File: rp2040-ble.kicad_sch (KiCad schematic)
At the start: 38 parts, among them J1 Conn_01x15, J2 Conn_01x15, J3 USB_B_Micro, J4 Conn_01x03, SW1 SW_Push, SW2 SW_Push, U1 RP2040, U2 W25Q128JVS, U3 HM-BT4502, U4 NCP1117DT33G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

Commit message: WIP Routing
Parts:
- removed R3: DNP, Resistor_SMD:R_0603_1608Metric, symbol Device:R_Small
- removed Y1: 12MHz, Crystal:Crystal_SMD_Abracon_ABM3-2Pin_5.0x3.2mm_HandSoldering, symbol Device:Crystal
- added H1, H2, H3, H4: MountingHole, MountingHole:MountingHole_2.2mm_M2, symbol Mechanical:MountingHole
- added Y1: ABLS-12.000MHZ-B4-T, ABLS-12:XTAL_ABLS-12.000MHZ-B4-T, symbol ABLS-12.000MHZ-B4-T:ABLS-12.000MHZ-B4-T
- C1, C10, C11, C12, C13, C14, C2, C3, C4, C5, C6, C7, C8, C9: footprint Capacitor_SMD:C_0603_1608Metric -> Capacitor_SMD:C_0402_1005Metric
- J1, J2: footprint Connector_PinSocket_1.27mm:PinSocket_1x15_P1.27mm_Vertical -> Connector_PinSocket_2.54mm:PinSocket_1x15_P2.54mm_Vertical
- J4: footprint Connector_PinSocket_1.27mm:PinSocket_1x03_P1.27mm_Vertical -> Connector_PinHeader_1.27mm:PinHeader_1x03_P1.27mm_Vertical
- R1, R2, R4, R5, R6, R7, R8: footprint Resistor_SMD:R_0603_1608Metric -> Resistor_SMD:R_0402_1005Metric
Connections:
- net BLE_INT: now also U1.14 (GPIO11); no longer U1.6 (GPIO4)
- net BLE_POWER_DOWN: now also U1.18 (GPIO15); no longer U1.5 (GPIO3)
- net BLE_RX: now also U1.15 (GPIO12); no longer U1.2 (GPIO0)
- net BLE_TX: now also U1.16 (GPIO13); no longer U1.3 (GPIO1)
- net BLE_WAKEUP: now also U1.17 (GPIO14); no longer U1.4 (GPIO2)
- net GND: now also J1.13 (Pin_13), J1.14 (Pin_14); no longer J2.14 (Pin_14), J2.3 (Pin_3), J2.4 (Pin_4)
- net GPIO10: now also J1.12 (Pin_12); no longer J1.6 (Pin_6)
- net GPIO16: now also J2.14 (Pin_14)
- net GPIO17: now also J2.13 (Pin_13); no longer J1.12 (Pin_12)
- net GPIO18: now also J2.12 (Pin_12); no longer J1.13 (Pin_13)
- net GPIO19: now also J2.11 (Pin_11); no longer J1.14 (Pin_14)
- net GPIO20: now also J2.10 (Pin_10); no longer J2.5 (Pin_5)
- net GPIO21: now also J2.9 (Pin_9); no longer J2.6 (Pin_6)
- net GPIO22: now also J2.8 (Pin_8); no longer J2.7 (Pin_7)
- net GPIO23: now also J2.7 (Pin_7); no longer J2.8 (Pin_8)
- net GPIO24: now also J2.6 (Pin_6); no longer J2.9 (Pin_9)
- net GPIO26: now also J2.5 (Pin_5); no longer J2.10 (Pin_10)
- net GPIO27: now also J2.4 (Pin_4); no longer J2.11 (Pin_11)
- net GPIO28: now also J2.3 (Pin_3); no longer J2.12 (Pin_12)
- net GPIO29: now also J2.1 (Pin_1); no longer J2.13 (Pin_13)
- net GPIO5: now also J1.7 (Pin_7); no longer J1.1 (Pin_1)
- net GPIO6: now also J1.8 (Pin_8); no longer J1.2 (Pin_2)
- net GPIO7: now also J1.9 (Pin_9); no longer J1.3 (Pin_3)
- net GPIO8: now also J1.10 (Pin_10); no longer J1.4 (Pin_4)
- net GPIO9: now also J1.11 (Pin_11); no longer J1.5 (Pin_5)
- net SWCLK: now also J4.3 (Pin_3); no longer J4.1 (Pin_1)
- net SWD: now also J4.1 (Pin_1); no longer J4.3 (Pin_3)
- net VBUS: now also J1.1 (Pin_1); no longer J2.1 (Pin_1)
- net XIN: now also Y1.1
- net at C13.1, R4.2: now also Y1.2
- removed net GPIO11: J1.7 (Pin_7), U1.14 (GPIO11)
- removed net GPIO12: J1.8 (Pin_8), U1.15 (GPIO12)
- removed net GPIO13: J1.9 (Pin_9), U1.16 (GPIO13)
- removed net GPIO14: J1.10 (Pin_10), U1.17 (GPIO14)
- removed net GPIO15: J1.11 (Pin_11), U1.18 (GPIO15)
- new net GPIO0: J1.2 (Pin_2), U1.2 (GPIO0)
- new net GPIO1: J1.3 (Pin_3), U1.3 (GPIO1)
- new net GPIO2: J1.4 (Pin_4), U1.4 (GPIO2)
- new net GPIO3: J1.5 (Pin_5), U1.5 (GPIO3)
- new net GPIO4: J1.6 (Pin_6), U1.6 (GPIO4)
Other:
- note added: "Make sure R1 and R2 are close to RP2040"
- note added: "Mounting holes"
- note added: "SWD Connector"
- note removed: "Debug connector"
- moved on the sheet: C10, C13, R4

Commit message: PCB roouting
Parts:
- removed SW1, SW2: SW_Push, Button_Switch_SMD:SW_SPST_B3S-1000, symbol Switch:SW_Push
- added SW1, SW2: PTS810_SJK_250_SMTR_LFS, PTS810:PTS810 SJK 250 SMTR LFS, symbol PTS810:PTS810_SJK_250_SMTR_LFS
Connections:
- net +3.3V: now also J2.1 (Pin_1); no longer J2.2 (Pin_2)
- net GND: now also SW1.3, SW1.4, SW2.3, SW2.4
- net GPIO29: now also J2.2 (Pin_2); no longer J2.1 (Pin_1)
- net RUN: now also SW2.1, SW2.2
- net USB_BOOT: now reaches R6.2
- net USB_BOOT: now also SW1.1, SW1.2
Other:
- note added: "Bootsel"
- note added: "Buttons"
- note added: "Connectors"
- note added: "Reset"
- note removed: "Reset Button"
- moved on the sheet: C14, H1, H2, H3, H4, J1, J2, J4, R6, R8, U2

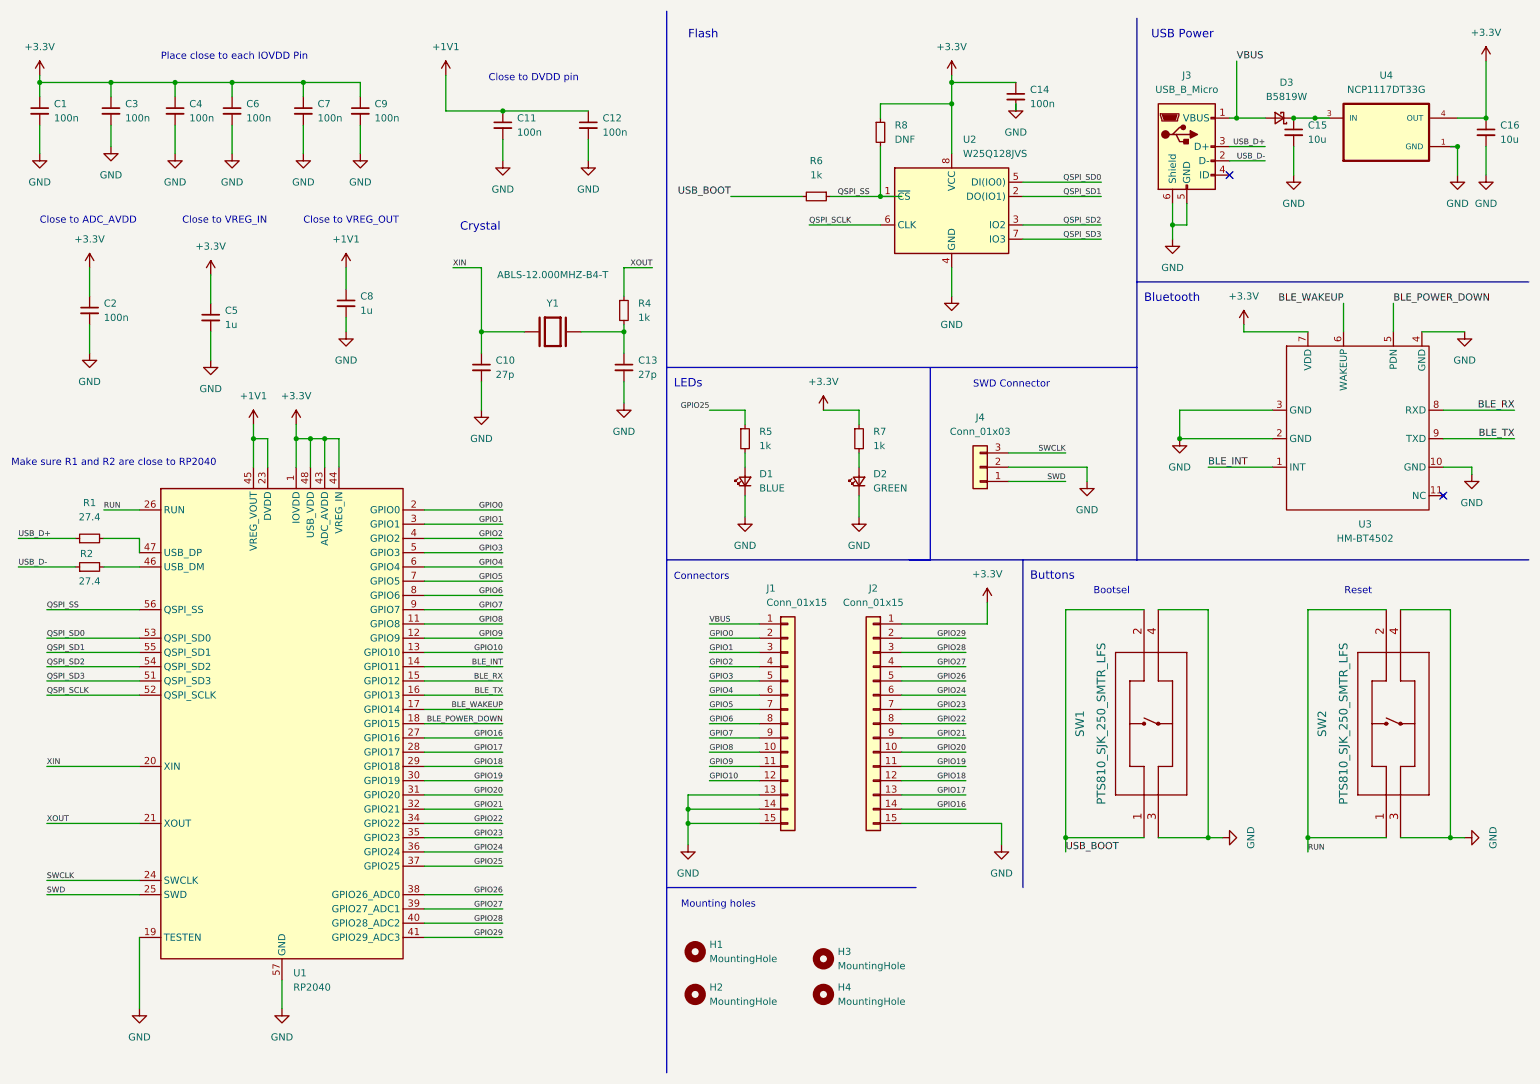
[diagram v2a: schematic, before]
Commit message: Updated routing, addedd 3d models for parts
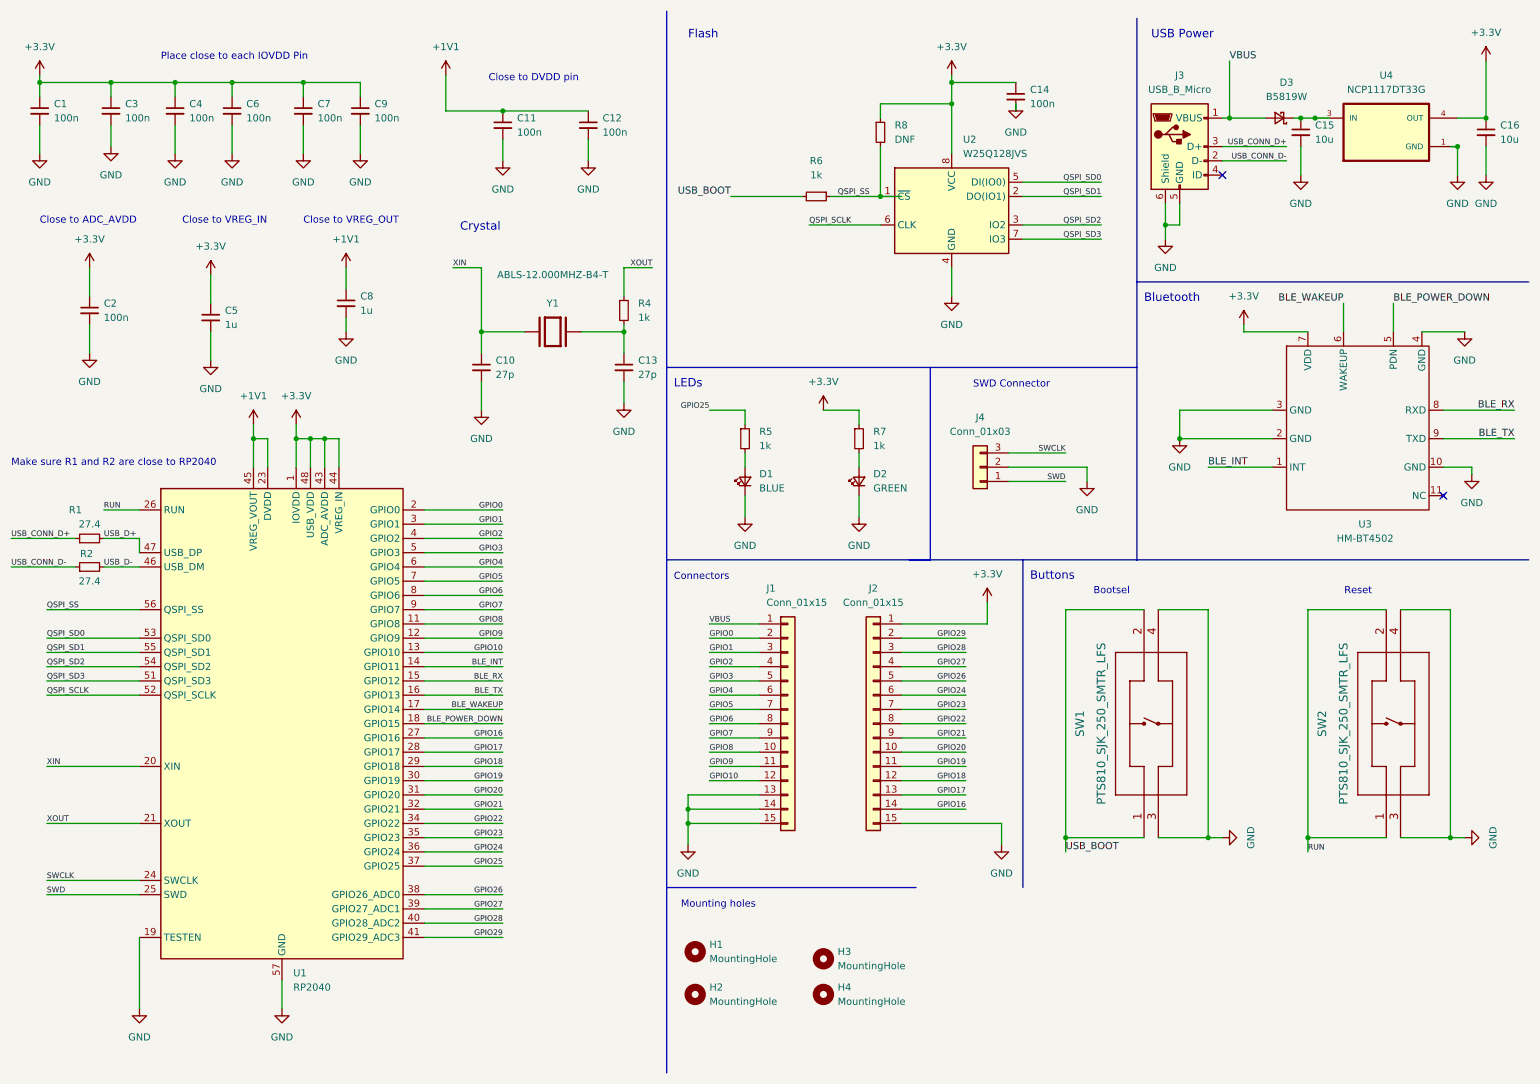
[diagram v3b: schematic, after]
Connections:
- net USB_D+: now also R1.2, U1.47 (USB_DP); no longer J3.3 (D+), R1.1
- net USB_D-: now also R2.2, U1.46 (USB_DM); no longer J3.2 (D-), R2.1
- new net USB_CONN_D+: J3.3 (D+), R1.1
- new net USB_CONN_D-: J3.2 (D-), R2.1
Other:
- moved on the sheet: C15, J3

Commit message: Add gerbers, fix pcb issues
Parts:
- R1, R2, R4, R5, R6, R7, R8: footprint Resistor_SMD:R_0402_1005Metric -> Resistor_SMD:R_0603_1608Metric
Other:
- title: (none) -> RP2040 BLE
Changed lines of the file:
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@@
 (kicad_sch (version 20211123) (generator eeschema)
   (paper "A4")
+  (title_block
+    (title "RP2040 BLE")
+    (date "2022-08-27")
+    (rev "v1")
+    (comment 2 "https://creativecommons.org/licenses/by/4.0/")
+    (comment 3 "License: CC BY 4.0")
+    (comment 4 "Author: Kartik Malik")
+  )
   (junction (at 135.89 154.94) (diameter 0) (color 0 0 0 0)
   )
@@
       (effects (font (size 1.27 1.27)) (justify left))
     )
-    (property "Footprint" "Resistor_SMD:R_0402_1005Metric" (id 2) (at 170.18 31.75 0)
+    (property "Footprint" "Resistor_SMD:R_0603_1608Metric" (id 2) (at 170.18 31.75 0)
       (effects (font (size 1.27 1.27)) hide)
     )
@@
     (property "Reference" "R6" (id 0) (at 158.75 36.83 90))
     (property "Value" "1k" (id 1) (at 158.75 39.37 90))
-    (property "Footprint" "Resistor_SMD:R_0402_1005Metric" (id 2) (at 158.75 43.18 0)
+    (property "Footprint" "Resistor_SMD:R_0603_1608Metric" (id 2) (at 158.75 43.18 0)
       (effects (font (size 1.27 1.27)) hide)
     )
@@
     (property "Reference" "R1" (id 0) (at 26.67 99.06 90))
     (property "Value" "27.4" (id 1) (at 29.21 101.6 90))
-    (property "Footprint" "Resistor_SMD:R_0402_1005Metric" (id 2) (at 29.21 104.14 0)
+    (property "Footprint" "Resistor_SMD:R_0603_1608Metric" (id 2) (at 29.21 104.14 0)
       (effects (font (size 1.27 1.27)) hide)
     )
@@
       (effects (font (size 1.27 1.27)) (justify left))
     )
-    (property "Footprint" "Resistor_SMD:R_0402_1005Metric" (id 2) (at 166.37 86.36 0)
+    (property "Footprint" "Resistor_SMD:R_0603_1608Metric" (id 2) (at 166.37 86.36 0)
       (effects (font (size 1.27 1.27)) hide)
     )
@@
       (effects (font (size 1.27 1.27)) (justify left))
     )
-    (property "Footprint" "Resistor_SMD:R_0402_1005Metric" (id 2) (at 124.46 63.5 0)
+    (property "Footprint" "Resistor_SMD:R_0603_1608Metric" (id 2) (at 124.46 63.5 0)
       (effects (font (size 1.27 1.27)) hide)
     )
@@
       (effects (font (size 1.27 1.27)) (justify left))
     )
-    (property "Footprint" "Resistor_SMD:R_0402_1005Metric" (id 2) (at 146.05 86.36 0)
+    (property "Footprint" "Resistor_SMD:R_0603_1608Metric" (id 2) (at 146.05 86.36 0)
       (effects (font (size 1.27 1.27)) hide)
     )
@@
     (property "Reference" "R2" (id 0) (at 28.6697 106.8682 90))
     (property "Value" "27.4" (id 1) (at 29.21 111.76 90))
-    (property "Footprint" "Resistor_SMD:R_0402_1005Metric" (id 2) (at 29.21 109.22 0)
+    (property "Footprint" "Resistor_SMD:R_0603_1608Metric" (id 2) (at 29.21 109.22 0)
       (effects (font (size 1.27 1.27)) hide)
     )
@@
     )
     (path "/396cd95e-c51a-485e-8d27-e8b8f30a1b91"
-      (reference "R1") (unit 1) (value "27.4") (footprint "Resistor_SMD:R_0402_1005Metric")
+      (reference "R1") (unit 1) (value "27.4") (footprint "Resistor_SMD:R_0603_1608Metric")
     )
     (path "/ddc112ab-af65-4c6c-b634-b868e7861ce8"
-      (reference "R2") (unit 1) (value "27.4") (footprint "Resistor_SMD:R_0402_1005Metric")
+      (reference "R2") (unit 1) (value "27.4") (footprint "Resistor_SMD:R_0603_1608Metric")
     )
     (path "/be235b21-ee57-4d5c-af0b-89b0a19c4cea"
-      (reference "R4") (unit 1) (value "1k") (footprint "Resistor_SMD:R_0402_1005Metric")
+      (reference "R4") (unit 1) (value "1k") (footprint "Resistor_SMD:R_0603_1608Metric")
     )
     (path "/cc0f1680-b3c8-4d4d-abcc-50aa4f2eccdb"
-      (reference "R5") (unit 1) (value "1k") (footprint "Resistor_SMD:R_0402_1005Metric")
+      (reference "R5") (unit 1) (value "1k") (footprint "Resistor_SMD:R_0603_1608Metric")
     )
     (path "/2765ac31-1258-496d-868b-a8d79f385fb9"
-      (reference "R6") (unit 1) (value "1k") (footprint "Resistor_SMD:R_0402_1005Metric")
+      (reference "R6") (unit 1) (value "1k") (footprint "Resistor_SMD:R_0603_1608Metric")
     )
     (path "/95e74ba7-789b-4626-929d-5c80a3645439"
-      (reference "R7") (unit 1) (value "1k") (footprint "Resistor_SMD:R_0402_1005Metric")
+      (reference "R7") (unit 1) (value "1k") (footprint "Resistor_SMD:R_0603_1608Metric")
     )
     (path "/2152357c-0ad2-4b05-be58-aaf94923aea4"
-      (reference "R8") (unit 1) (value "DNF") (footprint "Resistor_SMD:R_0402_1005Metric")
+      (reference "R8") (unit 1) (value "DNF") (footprint "Resistor_SMD:R_0603_1608Metric")
     )
     (path "/097d2be6-1b1c-4e8c-8674-3a4512b0d1e4"

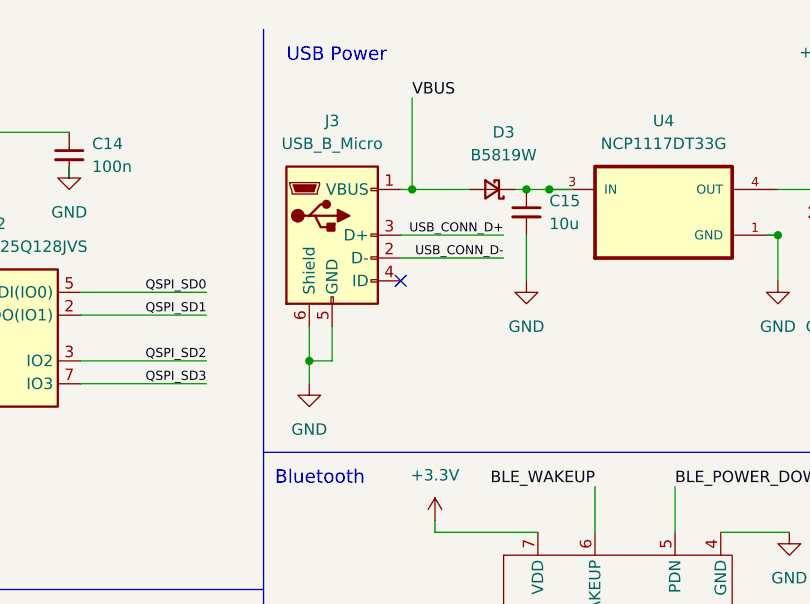
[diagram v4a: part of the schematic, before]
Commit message: Incorporate review feedback
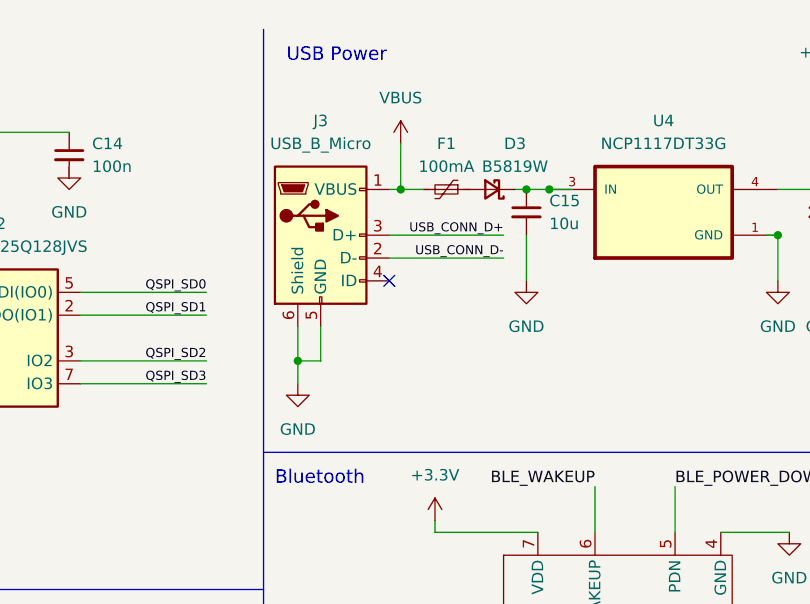
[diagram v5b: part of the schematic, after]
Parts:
- added F1: 100mA, Fuse:Fuse_0603_1608Metric, symbol Device:Polyfuse_Small
- R1, R2, R4, R5, R6, R7, R8: footprint Resistor_SMD:R_0603_1608Metric -> Resistor_SMD:R_0402_1005Metric
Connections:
- net VBUS: now also F1.2; no longer D3.2 (A)
- new net: D3.2 (A), F1.1
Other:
- moved on the sheet: J3
